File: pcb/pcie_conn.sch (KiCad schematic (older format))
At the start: 2 parts

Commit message: schematic completed. Time for review
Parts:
- added C? (x4): C, symbol C
- added FB?: FILTER, symbol FILTER
- added R? (x2): R, symbol R
- added TP? (x2): Test_Pad, symbol Test_Pad
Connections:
- net PCIE_PRSNT#1: now reaches J?.A1 (PRSNT#1)
- net PCIE_PRSNT#1: now also TP?.1
- net PERST#: now reaches J?.A11 (PERST#)
- net PERST#: now also R?.1, R?.2
- net GND: now reaches J?.A12 (GND)
- net GND: now also J?.A15 (GND), J?.A18 (GND), J?.A4 (GND), J?.B13 (GND), J?.B16 (GND), J?.B18 (GND), J?.B4 (GND), J?.B7 (GND), R?.2
- net PCIE_CLK_P: now reaches J?.A13 (REFCLK+)
- net PCIE_CLK_P: now also C?.1, C?.2
- net PCIE_CLK_N: now reaches J?.A14 (REFCLK-)
- net PCIE_CLK_N: now also C?.1, C?.2
- net PCIE_TX0_P: now reaches J?.A16 (HSIp(0))
- net PCIE_TX0_P: now also C?.1, C?.2
- net PCIE_TX0_N: now reaches J?.A17 (HSIn(0))
- net PCIE_TX0_N: now also J?.B15 (HSOn(0)), C?.1, C?.2
- net 12V: now reaches J?.A2 (12V0)
- net 12V: now also J?.A3 (12V0), J?.B1 (12V0), J?.B2 (12V0), J?.B3 (12V0), FB?.1
- net CLKREQ#: now reaches J?.B12 (CLKREQ#)
- net CLKREQ#: now also R?.1
- net PCIE_RX0_P: now reaches J?.B14 (HSOp(0))
- net PCIE_PRSNT#2: now reaches J?.B17 (PRSNT#2)
- net PCIE_PRSNT#2: now also TP?.1
- new net +12V: FB?.2
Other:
- note added: "Jumper for presence detect"

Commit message: Added part numbers and updated schematic
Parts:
- gave numbers to parts that had none: 10
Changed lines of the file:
@@
 $EndDescr
 $Comp
-L PCIe_x1 J?
+L PCIe_x1 J201
 U 1 1 561CA121
 P 2600 2750
-F 0 "J?" H 2400 3750 60  0000 C CNN
+F 0 "J201" H 2400 3750 60  0000 C CNN
 F 1 "PCIe_x1" H 2500 1750 60  0000 C CNN
 F 2 "" H 3050 2050 60  0000 C CNN
@@
 $EndComp
 $Comp
-L PCIe_x1 J?
+L PCIe_x1 J201
 U 2 1 561CA198
 P 2600 4950
-F 0 "J?" H 2400 5950 60  0000 C CNN
+F 0 "J201" H 2400 5950 60  0000 C CNN
 F 1 "PCIe_x1" H 2500 3950 60  0000 C CNN
 F 2 "" H 3050 4250 60  0000 C CNN
@@
 $EndComp
 $Comp
-L FILTER FB?
+L FILTER FB201
 U 1 1 5650A285
 P 6250 1600
-F 0 "FB?" H 6250 1750 50  0000 C CNN
+F 0 "FB201" H 6250 1750 50  0000 C CNN
 F 1 "FILTER" H 6250 1500 50  0000 C CNN
 F 2 "" H 6250 1600 60  0000 C CNN
@@
 	6700 1600 6700 1500
 $Comp
-L +12V #PWR?
+L +12V #PWR210
 U 1 1 5650A336
 P 6700 1500
-F 0 "#PWR?" H 6700 1350 50  0001 C CNN
+F 0 "#PWR210" H 6700 1350 50  0001 C CNN
 F 1 "+12V" H 6700 1640 50  0000 C CNN
 F 2 "" H 6700 1500 60  0000 C CNN
@@
 12V
 $Comp
-L GND #PWR?
+L GND #PWR205
 U 1 1 5650A392
 P 3500 4400
-F 0 "#PWR?" H 3500 4150 50  0001 C CNN
+F 0 "#PWR205" H 3500 4150 50  0001 C CNN
 F 1 "GND" H 3500 4250 50  0000 C CNN
 F 2 "" H 3500 4400 60  0000 C CNN
@@
 $EndComp
 $Comp
-L GND #PWR?
+L GND #PWR207
 U 1 1 5650A3AF
 P 3500 5300
-F 0 "#PWR?" H 3500 5050 50  0001 C CNN
+F 0 "#PWR207" H 3500 5050 50  0001 C CNN
 F 1 "GND" H 3500 5150 50  0000 C CNN
 F 2 "" H 3500 5300 60  0000 C CNN
@@
 $EndComp
 $Comp
-L GND #PWR?
+L GND #PWR209
 U 1 1 5650A3CC
 P 3500 5900
-F 0 "#PWR?" H 3500 5650 50  0001 C CNN
+F 0 "#PWR209" H 3500 5650 50  0001 C CNN
 F 1 "GND" H 3500 5750 50  0000 C CNN
 F 2 "" H 3500 5900 60  0000 C CNN
@@
 $EndComp
 $Comp
-L GND #PWR?
+L GND #PWR201
 U 1 1 5650A3E9
 P 3200 3700
-F 0 "#PWR?" H 3200 3450 50  0001 C CNN
+F 0 "#PWR201" H 3200 3450 50  0001 C CNN
 F 1 "GND" H 3200 3550 50  0000 C CNN
 F 2 "" H 3200 3700 60  0000 C CNN
@@
 $EndComp
 $Comp
-L GND #PWR?
+L GND #PWR202
 U 1 1 5650A406
 P 3500 2200
-F 0 "#PWR?" H 3500 1950 50  0001 C CNN
+F 0 "#PWR202" H 3500 1950 50  0001 C CNN
 F 1 "GND" H 3500 2050 50  0000 C CNN
 F 2 "" H 3500 2200 60  0000 C CNN
@@
 $EndComp
 $Comp
-L GND #PWR?
+L GND #PWR203
 U 1 1 5650A423
 P 3500 3000
-F 0 "#PWR?" H 3500 2750 50  0001 C CNN
+F 0 "#PWR203" H 3500 2750 50  0001 C CNN
 F 1 "GND" H 3500 2850 50  0000 C CNN
 F 2 "" H 3500 3000 60  0000 C CNN
@@
 $EndComp
 $Comp
-L GND #PWR?
+L GND #PWR204
 U 1 1 5650A440
 P 3500 3300
-F 0 "#PWR?" H 3500 3050 50  0001 C CNN
+F 0 "#PWR204" H 3500 3050 50  0001 C CNN
 F 1 "GND" H 3500 3150 50  0000 C CNN
 F 2 "" H 3500 3300 60  0000 C CNN
@@
 	3200 3600 3200 3700
 $Comp
-L GND #PWR?
+L GND #PWR206
 U 1 1 5650DC8E
 P 3500 4700
-F 0 "#PWR?" H 3500 4450 50  0001 C CNN
+F 0 "#PWR206" H 3500 4450 50  0001 C CNN
 F 1 "GND" H 3500 4550 50  0000 C CNN
 F 2 "" H 3500 4700 60  0000 C CNN
@@
 	3100 4700 3500 4700
 $Comp
-L GND #PWR?
+L GND #PWR208
 U 1 1 5650DCCC
 P 3500 5600
-F 0 "#PWR?" H 3500 5350 50  0001 C CNN
+F 0 "#PWR208" H 3500 5350 50  0001 C CNN
 F 1 "GND" H 3500 5450 50  0000 C CNN
 F 2 "" H 3500 5600 60  0000 C CNN
@@
 PCIE_RX0_P
 $Comp
-L C C?
+L C C203
 U 1 1 565105FE
 P 7450 3300
-F 0 "C?" H 7475 3400 50  0000 L CNN
+F 0 "C203" H 7475 3400 50  0000 L CNN
 F 1 "C" H 7475 3200 50  0000 L CNN
 F 2 "" H 7488 3150 30  0000 C CNN
@@
 $EndComp
 $Comp
-L C C?
+L C C204
 U 1 1 5651066D
 P 7450 3500
-F 0 "C?" H 7475 3600 50  0000 L CNN
+F 0 "C204" H 7475 3600 50  0000 L CNN
 F 1 "C" H 7475 3400 50  0000 L CNN
 F 2 "" H 7488 3350 30  0000 C CNN
@@
 $EndComp
 $Comp
-L C C?
+L C C201
 U 1 1 565106AB
 P 7450 2800
-F 0 "C?" H 7475 2900 50  0000 L CNN
+F 0 "C201" H 7475 2900 50  0000 L CNN
 F 1 "C" H 7475 2700 50  0000 L CNN
 F 2 "" H 7488 2650 30  0000 C CNN
@@
 $EndComp
 $Comp
-L C C?
+L C C202
 U 1 1 565106F6
 P 7450 3000
-F 0 "C?" H 7475 3100 50  0000 L CNN
+F 0 "C202" H 7475 3100 50  0000 L CNN
 F 1 "C" H 7475 2900 50  0000 L CNN
 F 2 "" H 7488 2850 30  0000 C CNN
@@
 PCIE_PRSNT#2
 $Comp
-L Test_Pad TP?
+L Test_Pad TP201
 U 1 1 56510AB0
 P 6400 5500
-F 0 "TP?" H 6600 5500 60  0000 C CNN
+F 0 "TP201" H 6600 5500 60  0000 C CNN
 F 1 "Test_Pad" H 6350 5650 60  0001 C CNN
 F 2 "" H 6400 5500 60  0000 C CNN
@@
 $EndComp
 $Comp
-L Test_Pad TP?
+L Test_Pad TP202
 U 1 1 56510AF7
 P 6400 5700
-F 0 "TP?" H 6600 5700 60  0000 C CNN
+F 0 "TP202" H 6600 5700 60  0000 C CNN
 F 1 "Test_Pad" H 6350 5850 60  0001 C CNN
 F 2 "" H 6400 5700 60  0000 C CNN
@@
 CLKREQ#
 $Comp
-L R R?
+L R R202
 U 1 1 565110AB
 P 9900 4150
-F 0 "R?" V 9980 4150 50  0000 C CNN
+F 0 "R202" V 9980 4150 50  0000 C CNN
 F 1 "R" V 9900 4150 50  0000 C CNN
 F 2 "" V 9830 4150 30  0000 C CNN
@@
 	9900 3800 9700 3800
 $Comp
-L GND #PWR?
+L GND #PWR211
 U 1 1 56511671
 P 9900 4500
-F 0 "#PWR?" H 9900 4250 50  0001 C CNN
+F 0 "#PWR211" H 9900 4250 50  0001 C CNN
 F 1 "GND" H 9900 4350 50  0000 C CNN
 F 2 "" H 9900 4500 60  0000 C CNN
@@
 PERST#
 $Comp
-L R R?
+L R R201
 U 1 1 56511788
 P 7450 4200
-F 0 "R?" V 7530 4200 50  0000 C CNN
+F 0 "R201" V 7530 4200 50  0000 C CNN
 F 1 "R" V 7450 4200 50  0000 C CNN
 F 2 "" V 7380 4200 30  0000 C CNN

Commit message: mostly done with component placement
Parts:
- added F201: FUSE, wbraun_smd:SMD-0805, symbol FUSE
- C201, C202, C203, C204: value C -> 0.22uF; footprint (none) -> wbraun_smd:C_0402
- FB201: footprint (none) -> wbraun_smd:L_0603
- J201: footprint (none) -> wbraun_smd:PCIe_1x
- R201, R202: footprint (none) -> wbraun_smd:R_0402
- TP201, TP202: footprint (none) -> Wire_Pads:SolderWirePad_single_0-8mmDrill
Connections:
- net +12V: now also F201.2; no longer FB201.2
- net PCIE_CLK_N: no longer C202.2, J201.A14 (REFCLK-)
- net PCIE_CLK_P: no longer C201.2, J201.A13 (REFCLK+)
- net PCIE_RX0_N: now also J201.B15 (HSOn(0))
- net PCIE_TX0_N: no longer C204.2, J201.A17 (HSIn(0)), J201.B15 (HSOn(0))
- net PCIE_TX0_P: no longer C203.2, J201.A16 (HSIp(0))
- net PERST#: no longer J201.A11 (PERST#), R201.2
- net 12V renamed 12V_power
- new net: F201.1, FB201.2
- new net PCIE_CLK_C_N: C202.2, J201.A14 (REFCLK-)
- new net PCIE_CLK_C_P: C201.2, J201.A13 (REFCLK+)
- new net PCIE_TX0_C_N: C204.2, J201.A17 (HSIn(0))
- new net PCIE_TX0_C_P: C203.2, J201.A16 (HSIp(0))
- new net PERST#R: J201.A11 (PERST#), R201.2
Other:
- note added: "1 Amp hold current, 1210"
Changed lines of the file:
@@
 F 0 "J201" H 2400 3750 60  0000 C CNN
 F 1 "PCIe_x1" H 2500 1750 60  0000 C CNN
-F 2 "" H 3050 2050 60  0000 C CNN
+F 2 "wbraun_smd:PCIe_1x" H 3050 2050 60  0001 C CNN
 F 3 "" H 3050 2050 60  0000 C CNN
 	1    2600 2750
@@
 F 0 "J201" H 2400 5950 60  0000 C CNN
 F 1 "PCIe_x1" H 2500 3950 60  0000 C CNN
-F 2 "" H 3050 4250 60  0000 C CNN
+F 2 "wbraun_smd:PCIe_1x" H 3050 4250 60  0001 C CNN
 F 3 "" H 3050 4250 60  0000 C CNN
 	2    2600 4950
@@
 F 0 "FB201" H 6250 1750 50  0000 C CNN
 F 1 "FILTER" H 6250 1500 50  0000 C CNN
-F 2 "" H 6250 1600 60  0000 C CNN
+F 2 "wbraun_smd:L_0603" H 6250 1600 60  0001 C CNN
 F 3 "" H 6250 1600 60  0000 C CNN
 	1    6250 1600
@@
 	5900 1600 5800 1600
 Wire Wire Line
-	6600 1600 6700 1600
-Wire Wire Line
-	6700 1600 6700 1500
-$Comp
-L +12V #PWR210
+	7200 1600 7400 1600
+Wire Wire Line
+	7400 1600 7400 1500
+$Comp
+L +12V #PWR01
 U 1 1 5650A336
-P 6700 1500
-F 0 "#PWR210" H 6700 1350 50  0001 C CNN
-F 1 "+12V" H 6700 1640 50  0000 C CNN
-F 2 "" H 6700 1500 60  0000 C CNN
-F 3 "" H 6700 1500 60  0000 C CNN
-	1    6700 1500
+P 7400 1500
+F 0 "#PWR01" H 7400 1350 50  0001 C CNN
+F 1 "+12V" H 7400 1640 50  0000 C CNN
+F 2 "" H 7400 1500 60  0000 C CNN
+F 3 "" H 7400 1500 60  0000 C CNN
+	1    7400 1500
 	1    0    0    -1
 $EndComp
 Text Label 5800 1600 2    60   ~ 0
-12V
+12V_power
 Text Label 3300 2000 0    60   ~ 0
-12V
+12V_power
 Text Label 3300 4100 0    60   ~ 0
-12V
-$Comp
-L GND #PWR205
+12V_power
+$Comp
+L GND #PWR02
 U 1 1 5650A392
 P 3500 4400
-F 0 "#PWR205" H 3500 4150 50  0001 C CNN
+F 0 "#PWR02" H 3500 4150 50  0001 C CNN
 F 1 "GND" H 3500 4250 50  0000 C CNN
 F 2 "" H 3500 4400 60  0000 C CNN
@@
 $EndComp
 $Comp
-L GND #PWR207
+L GND #PWR03
 U 1 1 5650A3AF
 P 3500 5300
-F 0 "#PWR207" H 3500 5050 50  0001 C CNN
+F 0 "#PWR03" H 3500 5050 50  0001 C CNN
 F 1 "GND" H 3500 5150 50  0000 C CNN
 F 2 "" H 3500 5300 60  0000 C CNN
@@
 $EndComp
 $Comp
-L GND #PWR209
+L GND #PWR04
 U 1 1 5650A3CC
 P 3500 5900
-F 0 "#PWR209" H 3500 5650 50  0001 C CNN
+F 0 "#PWR04" H 3500 5650 50  0001 C CNN
 F 1 "GND" H 3500 5750 50  0000 C CNN
 F 2 "" H 3500 5900 60  0000 C CNN
@@
 $EndComp
 $Comp
-L GND #PWR201
+L GND #PWR05
 U 1 1 5650A3E9
 P 3200 3700
-F 0 "#PWR201" H 3200 3450 50  0001 C CNN
+F 0 "#PWR05" H 3200 3450 50  0001 C CNN
 F 1 "GND" H 3200 3550 50  0000 C CNN
 F 2 "" H 3200 3700 60  0000 C CNN
@@
 $EndComp
 $Comp
-L GND #PWR202
+L GND #PWR06
 U 1 1 5650A406
 P 3500 2200
-F 0 "#PWR202" H 3500 1950 50  0001 C CNN
+F 0 "#PWR06" H 3500 1950 50  0001 C CNN
 F 1 "GND" H 3500 2050 50  0000 C CNN
 F 2 "" H 3500 2200 60  0000 C CNN
@@
 $EndComp
 $Comp
-L GND #PWR203
+L GND #PWR07
 U 1 1 5650A423
 P 3500 3000
-F 0 "#PWR203" H 3500 2750 50  0001 C CNN
+F 0 "#PWR07" H 3500 2750 50  0001 C CNN
 F 1 "GND" H 3500 2850 50  0000 C CNN
 F 2 "" H 3500 3000 60  0000 C CNN
@@
 $EndComp
 $Comp
-L GND #PWR204
+L GND #PWR08
 U 1 1 5650A440
 P 3500 3300
-F 0 "#PWR204" H 3500 3050 50  0001 C CNN
+F 0 "#PWR08" H 3500 3050 50  0001 C CNN
 F 1 "GND" H 3500 3150 50  0000 C CNN
 F 2 "" H 3500 3300 60  0000 C CNN
@@
 	3200 3600 3200 3700
 $Comp
-L GND #PWR206
+L GND #PWR09
 U 1 1 5650DC8E
 P 3500 4700
-F 0 "#PWR206" H 3500 4450 50  0001 C CNN
+F 0 "#PWR09" H 3500 4450 50  0001 C CNN
 F 1 "GND" H 3500 4550 50  0000 C CNN
 F 2 "" H 3500 4700 60  0000 C CNN
@@
 	3100 4700 3500 4700
 $Comp
-L GND #PWR208
+L GND #PWR010
 U 1 1 5650DCCC
 P 3500 5600
-F 0 "#PWR208" H 3500 5350 50  0001 C CNN
+F 0 "#PWR010" H 3500 5350 50  0001 C CNN
 F 1 "GND" H 3500 5450 50  0000 C CNN
 F 2 "" H 3500 5600 60  0000 C CNN
@@
 	3100 3200 3200 3200
 Text Label 3200 3400 0    60   ~ 0
-PCIE_TX0_P
+PCIE_TX0_C_P
 Text Label 3200 3500 0    60   ~ 0
-PCIE_TX0_N
+PCIE_TX0_C_N
 Text Label 3200 5400 0    60   ~ 0
 PCIE_RX0_P
 Text Label 3200 5500 0    60   ~ 0
-PCIE_TX0_N
+PCIE_RX0_N
 Text Label 3200 3100 0    60   ~ 0
-PCIE_CLK_P
+PCIE_CLK_C_P
 Text Label 3200 3200 0    60   ~ 0
-PCIE_CLK_N
+PCIE_CLK_C_N
 Text HLabel 7800 2800 2    60   Input ~ 0
 PCIE_CLK_P
@@
 P 7450 3300
 F 0 "C203" H 7475 3400 50  0000 L CNN
-F 1 "C" H 7475 3200 50  0000 L CNN
-F 2 "" H 7488 3150 30  0000 C CNN
+F 1 "0.22uF" H 7475 3200 50  0000 L CNN
+F 2 "wbraun_smd:C_0402" H 7488 3150 30  0001 C CNN
 F 3 "" H 7450 3300 60  0000 C CNN
 	1    7450 3300
@@
 P 7450 3500
 F 0 "C204" H 7475 3600 50  0000 L CNN
-F 1 "C" H 7475 3400 50  0000 L CNN
-F 2 "" H 7488 3350 30  0000 C CNN
+F 1 "0.22uF" H 7475 3400 50  0000 L CNN
+F 2 "wbraun_smd:C_0402" H 7488 3350 30  0001 C CNN
 F 3 "" H 7450 3500 60  0000 C CNN
 	1    7450 3500
@@
 P 7450 2800
 F 0 "C201" H 7475 2900 50  0000 L CNN
-F 1 "C" H 7475 2700 50  0000 L CNN
-F 2 "" H 7488 2650 30  0000 C CNN
+F 1 "0.22uF" H 7475 2700 50  0000 L CNN
+F 2 "wbraun_smd:C_0402" H 7488 2650 30  0001 C CNN
 F 3 "" H 7450 2800 60  0000 C CNN
 	1    7450 2800
@@
 P 7450 3000
 F 0 "C202" H 7475 3100 50  0000 L CNN
-F 1 "C" H 7475 2900 50  0000 L CNN
-F 2 "" H 7488 2850 30  0000 C CNN
+F 1 "0.22uF" H 7475 2900 50  0000 L CNN
+F 2 "wbraun_smd:C_0402" H 7488 2850 30  0001 C CNN
 F 3 "" H 7450 3000 60  0000 C CNN
 	1    7450 3000
@@
 	7800 3950 7100 3950
 Text Label 7100 3300 2    60   ~ 0
-PCIE_TX0_P
+PCIE_TX0_C_P
 Text Label 7100 3500 2    60   ~ 0
-PCIE_TX0_N
+PCIE_TX0_C_N
 Text Label 7100 2800 2    60   ~ 0
-PCIE_CLK_P
+PCIE_CLK_C_P
 Text Label 7100 3000 2    60   ~ 0
-PCIE_CLK_N
+PCIE_CLK_C_N
 Text Label 7100 3800 2    60   ~ 0
 PCIE_RX0_P
@@
 F 0 "TP201" H 6600 5500 60  0000 C CNN
 F 1 "Test_Pad" H 6350 5650 60  0001 C CNN
-F 2 "" H 6400 5500 60  0000 C CNN
+F 2 "Wire_Pads:SolderWirePad_single_0-8mmDrill" H 6400 5500 60  0001 C CNN
 F 3 "" H 6400 5500 60  0000 C CNN
 	1    6400 5500
@@
 F 0 "TP202" H 6600 5700 60  0000 C CNN
 F 1 "Test_Pad" H 6350 5850 60  0001 C CNN
-F 2 "" H 6400 5700 60  0000 C CNN
+F 2 "Wire_Pads:SolderWirePad_single_0-8mmDrill" H 6400 5700 60  0001 C CNN
 F 3 "" H 6400 5700 60  0000 C CNN
 	1    6400 5700
@@
 F 0 "R202" V 9980 4150 50  0000 C CNN
 F 1 "R" V 9900 4150 50  0000 C CNN
-F 2 "" V 9830 4150 30  0000 C CNN
+F 2 "wbraun_smd:R_0402" V 9830 4150 30  0001 C CNN
 F 3 "" H 9900 4150 30  0000 C CNN
 	1    9900 4150
@@
 	9900 3800 9700 3800
 $Comp
-L GND #PWR211
+L GND #PWR011
 U 1 1 56511671
 P 9900 4500
-F 0 "#PWR211" H 9900 4250 50  0001 C CNN
+F 0 "#PWR011" H 9900 4250 50  0001 C CNN
 F 1 "GND" H 9900 4350 50  0000 C CNN
 F 2 "" H 9900 4500 60  0000 C CNN
@@
 PERST#
 Text Label 3200 2900 0    60   ~ 0
-PERST#
+PERST#R
 $Comp
 L R R201
@@
 F 0 "R201" V 7530 4200 50  0000 C CNN
 F 1 "R" V 7450 4200 50  0000 C CNN
-F 2 "" V 7380 4200 30  0000 C CNN
+F 2 "wbraun_smd:R_0402" V 7380 4200 30  0001 C CNN
 F 3 "" H 7450 4200 30  0000 C CNN
 	1    7450 4200
@@
 $EndComp
 Text Label 7100 4200 2    60   ~ 0
-PERST#
+PERST#R
 Wire Wire Line
 	7800 4200 7600 4200
@@
 Text Notes 6200 5950 0    60   ~ 0
 Jumper for presence detect
+$Comp
+L FUSE F201
+U 1 1 566148F3
+P 6950 1600
+F 0 "F201" H 7050 1650 50  0000 C CNN
+F 1 "FUSE" H 6850 1550 50  0000 C CNN
+F 2 "wbraun_smd:SMD-0805" H 6950 1600 60  0001 C CNN
+F 3 "" H 6950 1600 60  0000 C CNN
+	1    6950 1600
+	1    0    0    -1
+$EndComp
+Wire Wire Line
+	6600 1600 6700 1600
+Text Notes 6550 1850 0    60   ~ 0
+1 Amp hold current, 1210
 $EndSCHEMATC

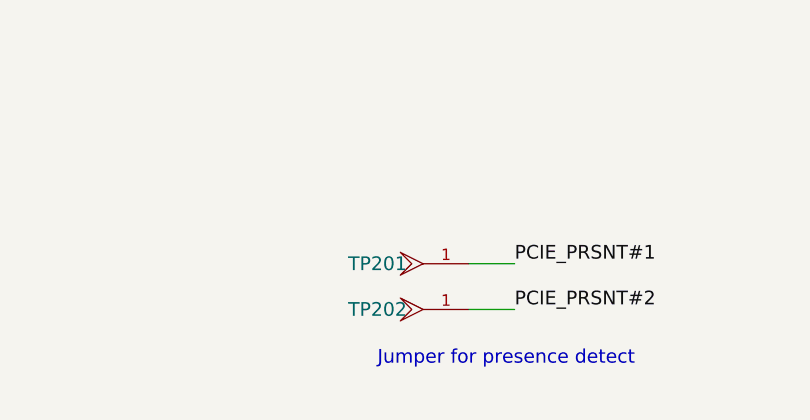
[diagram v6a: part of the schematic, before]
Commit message: routing finished, need final check
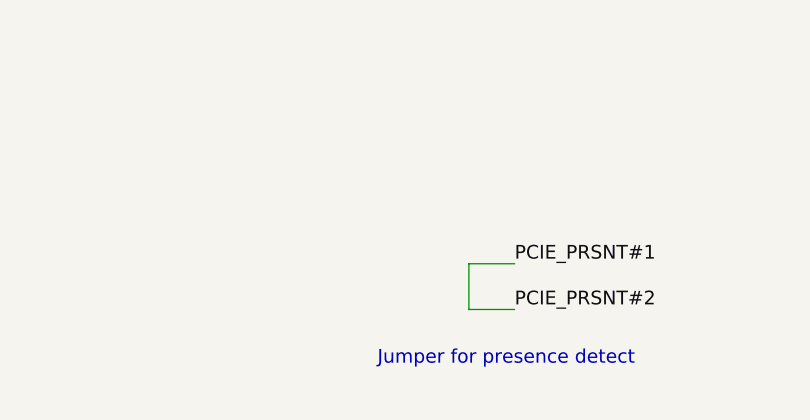
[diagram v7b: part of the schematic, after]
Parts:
- removed TP201, TP202: Test_Pad, Wire_Pads:SolderWirePad_single_0-8mmDrill, symbol Test_Pad
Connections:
- net PCIE_PRSNT#2 is gone; now on net PCIE_PRSNT#1: J201.B17 (PRSNT#2)
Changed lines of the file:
@@
 Text Label 6800 5700 0    60   ~ 0
 PCIE_PRSNT#2
-$Comp
-L Test_Pad TP201
-U 1 1 56510AB0
-P 6400 5500
-F 0 "TP201" H 6600 5500 60  0000 C CNN
-F 1 "Test_Pad" H 6350 5650 60  0001 C CNN
-F 2 "Wire_Pads:SolderWirePad_single_0-8mmDrill" H 6400 5500 60  0001 C CNN
-F 3 "" H 6400 5500 60  0000 C CNN
-	1    6400 5500
-	-1   0    0    1
-$EndComp
-$Comp
-L Test_Pad TP202
-U 1 1 56510AF7
-P 6400 5700
-F 0 "TP202" H 6600 5700 60  0000 C CNN
-F 1 "Test_Pad" H 6350 5850 60  0001 C CNN
-F 2 "Wire_Pads:SolderWirePad_single_0-8mmDrill" H 6400 5700 60  0001 C CNN
-F 3 "" H 6400 5700 60  0000 C CNN
-	1    6400 5700
-	-1   0    0    1
-$EndComp
 Wire Wire Line
 	6600 5500 6800 5500
@@
 Text Notes 6550 1850 0    60   ~ 0
 1 Amp hold current, 1210
+Wire Wire Line
+	6600 5500 6600 5700
 $EndSCHEMATC
